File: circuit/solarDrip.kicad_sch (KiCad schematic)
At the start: 51 parts, among them J1 solar_charger, J10 Conn_01x08_Socket, J11 Logo_bot, J12 Logo_µc3, J13 solar_charger_smd, J2 batt, J3 solar, J4 pump, J5 soil, J6 water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

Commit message: resize R1-R4 to 0306
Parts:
- R1, R2, R3, R4: footprint Resistor_SMD:R_0402_1005Metric_Pad0.72x0.64mm_HandSolder -> Resistor_SMD:R_0603_1608Metric_Pad0.98x0.95mm_HandSolder
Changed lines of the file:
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@@
 			)
 		)
-		(property "Footprint" "Resistor_SMD:R_0402_1005Metric_Pad0.72x0.64mm_HandSolder"
+		(property "Footprint" "Resistor_SMD:R_0603_1608Metric_Pad0.98x0.95mm_HandSolder"
 			(at 66.802 123.19 90)
 			(effects
@@
 			)
 		)
-		(property "Footprint" "Resistor_SMD:R_0402_1005Metric_Pad0.72x0.64mm_HandSolder"
+		(property "Footprint" "Resistor_SMD:R_0603_1608Metric_Pad0.98x0.95mm_HandSolder"
 			(at 38.862 115.57 90)
 			(effects
@@
 			)
 		)
-		(property "Footprint" "Resistor_SMD:R_0402_1005Metric_Pad0.72x0.64mm_HandSolder"
+		(property "Footprint" "Resistor_SMD:R_0603_1608Metric_Pad0.98x0.95mm_HandSolder"
 			(at 38.862 123.19 90)
 			(effects
@@
 			)
 		)
-		(property "Footprint" "Resistor_SMD:R_0402_1005Metric_Pad0.72x0.64mm_HandSolder"
+		(property "Footprint" "Resistor_SMD:R_0603_1608Metric_Pad0.98x0.95mm_HandSolder"
 			(at 66.802 115.57 90)
 			(effects

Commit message: resize R5-R9 to 0306
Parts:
- R5, R6, R7, R8, R9: footprint Resistor_SMD:R_0402_1005Metric_Pad0.72x0.64mm_HandSolder -> Resistor_SMD:R_0603_1608Metric_Pad0.98x0.95mm_HandSolder
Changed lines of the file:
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@@
 			)
 		)
-		(property "Footprint" "Resistor_SMD:R_0402_1005Metric_Pad0.72x0.64mm_HandSolder"
+		(property "Footprint" "Resistor_SMD:R_0603_1608Metric_Pad0.98x0.95mm_HandSolder"
 			(at 154.178 96.52 90)
 			(effects
@@
 			)
 		)
-		(property "Footprint" "Resistor_SMD:R_0402_1005Metric_Pad0.72x0.64mm_HandSolder"
+		(property "Footprint" "Resistor_SMD:R_0603_1608Metric_Pad0.98x0.95mm_HandSolder"
 			(at 256.032 114.3 90)
 			(effects
@@
 			)
 		)
-		(property "Footprint" "Resistor_SMD:R_0402_1005Metric_Pad0.72x0.64mm_HandSolder"
+		(property "Footprint" "Resistor_SMD:R_0603_1608Metric_Pad0.98x0.95mm_HandSolder"
 			(at 211.582 115.57 90)
 			(effects
@@
 			)
 		)
-		(property "Footprint" "Resistor_SMD:R_0402_1005Metric_Pad0.72x0.64mm_HandSolder"
+		(property "Footprint" "Resistor_SMD:R_0603_1608Metric_Pad0.98x0.95mm_HandSolder"
 			(at 147.32 93.218 90)
 			(effects
@@
 			)
 		)
-		(property "Footprint" "Resistor_SMD:R_0402_1005Metric_Pad0.72x0.64mm_HandSolder"
+		(property "Footprint" "Resistor_SMD:R_0603_1608Metric_Pad0.98x0.95mm_HandSolder"
 			(at 220.472 115.57 90)
 			(effects

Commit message: add logo symbols
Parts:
- J11, J12: symbol Connector:Conn_01x01_Pin -> logos:logo
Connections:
- net GND: no longer J11.1 (Pin_1), J12.1 (Pin_1)
- no-connect marks 4 -> 5
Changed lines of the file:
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@@
 		(at 209.55 114.3)
 	)
+	(no_connect
+		(at 269.24 151.13)
+	)
 	(wire
 		(pts
@@
 	)
 	(symbol
-		(lib_id "Connector:Conn_01x01_Pin")
-		(at 247.65 151.13 0)
+		(lib_id "logos:logo")
+		(at 238.76 149.86 0)
 		(unit 1)
 		(exclude_from_sim no)
@@
 		(on_board yes)
 		(dnp no)
-		(fields_autoplaced yes)
 		(property "Reference" "J11"
-			(at 248.285 146.05 0)
+			(at 242.57 148.5899 0)
 			(effects
 				(font
 					(size 1.27 1.27)
 				)
+				(justify left)
 			)
 		)
 		(property "Value" "Logo_bot"
-			(at 248.285 148.59 0)
+			(at 234.442 146.05 0)
 			(effects
 				(font
 					(size 1.27 1.27)
 				)
+				(justify left)
 			)
 		)
 		(property "Footprint" "my_footprints:logo_solardrip"
-			(at 247.65 151.13 0)
+			(at 238.76 149.86 0)
 			(effects
 				(font
@@
 		)
 		(property "Datasheet" "~"
-			(at 247.65 151.13 0)
+			(at 238.76 149.86 0)
 			(effects
 				(font
@@
 		)
 		(property "Description" "Generic connector, single row, 01x01, script generated"
-			(at 247.65 151.13 0)
+			(at 238.76 149.86 0)
 			(effects
 				(font
@@
 			)
 		)
-		(pin "1"
-		)
 		(instances
 			(project "solarDrip"
@@
 	)
 	(symbol
-		(lib_id "Connector:Conn_01x01_Pin")
-		(at 264.16 151.13 0)
+		(lib_id "logos:logo")
+		(at 251.46 149.86 0)
 		(unit 1)
 		(exclude_from_sim no)
@@
 		(on_board yes)
 		(dnp no)
-		(fields_autoplaced yes)
 		(property "Reference" "J12"
-			(at 264.795 146.05 0)
+			(at 255.27 148.5899 0)
 			(effects
 				(font
 					(size 1.27 1.27)
 				)
+				(justify left)
 			)
 		)
 		(property "Value" "Logo_µc3"
-			(at 264.795 148.59 0)
+			(at 247.65 146.05 0)
 			(effects
 				(font
 					(size 1.27 1.27)
 				)
+				(justify left)
 			)
 		)
 		(property "Footprint" "my_footprints:muccc_logo"
-			(at 264.16 151.13 0)
+			(at 251.46 149.86 0)
 			(effects
 				(font
@@
 		)
 		(property "Datasheet" "~"
-			(at 264.16 151.13 0)
+			(at 251.46 149.86 0)
 			(effects
 				(font
@@
 		)
 		(property "Description" "Generic connector, single row, 01x01, script generated"
-			(at 264.16 151.13 0)
+			(at 251.46 149.86 0)
 			(effects
 				(font
@@
 			)
 		)
-		(pin "1"
-		)
 		(instances
 			(project "solarDrip"
@@
 	)
 	(symbol
-		(lib_id "power:GND")
-		(at 269.24 151.13 0)
-		(unit 1)
-		(exclude_from_sim no)
-		(in_bom yes)
-		(on_board yes)
-		(dnp no)
-		(property "Reference" "#PWR023"
-			(at 269.24 157.48 0)
-			(effects
-				(font
-					(size 1.27 1.27)
-				)
-				(hide yes)
-			)
-		)
-		(property "Value" "GND"
-			(at 269.24 156.21 0)
-			(effects
-				(font
-					(size 1.27 1.27)
-				)
-			)
-		)
-		(property "Footprint" ""
-			(at 269.24 151.13 0)
-			(effects
-				(font
-					(size 1.27 1.27)
-				)
-				(hide yes)
-			)
-		)
-		(property "Datasheet" ""
-			(at 269.24 151.13 0)
-			(effects
-				(font
-					(size 1.27 1.27)
-				)
-				(hide yes)
-			)
-		)
-		(property "Description" "Power symbol creates a global label with name \"GND\" , ground"
-			(at 269.24 151.13 0)
-			(effects
-				(font
-					(size 1.27 1.27)
-				)
-				(hide yes)
-			)
-		)
-		(pin "1"
-		)
-		(instances
-			(project "solarDrip"
-				(path "/6377a484-fa16-4056-97a2-452f2b7af807"
-					(reference "#PWR023")
-					(unit 1)
-				)
-			)
-		)
-	)
-	(symbol
 		(lib_id "Device:R")
 		(at 40.64 123.19 0)
@@
 					(unit 1)
 				)
-			)
-		)
-	)
-	(symbol
-		(lib_id "power:GND")
-		(at 252.73 151.13 0)
-		(unit 1)
-		(exclude_from_sim no)
-		(in_bom yes)
-		(on_board yes)
-		(dnp no)
-		(property "Reference" "#PWR022"
-			(at 252.73 157.48 0)
-			(effects
-				(font
-					(size 1.27 1.27)
-				)
-				(hide yes)
-			)
-		)
-		(property "Value" "GND"
-			(at 252.73 156.21 0)
-			(effects
-				(font
-					(size 1.27 1.27)
-				)
-			)
-		)
-		(property "Footprint" ""
-			(at 252.73 151.13 0)
-			(effects
-				(font
-					(size 1.27 1.27)
-				)
-				(hide yes)
-			)
-		)
-		(property "Datasheet" ""
-			(at 252.73 151.13 0)
-			(effects
-				(font
-					(size 1.27 1.27)
-				)
-				(hide yes)
-			)
-		)
-		(property "Description" "Power symbol creates a global label with name \"GND\" , ground"
-			(at 252.73 151.13 0)
-			(effects
-				(font
-					(size 1.27 1.27)
-				)
-				(hide yes)
-			)
-		)
-		(pin "1"
-		)
-		(instances
-			(project "solarDrip"
-				(path "/6377a484-fa16-4056-97a2-452f2b7af807"
-					(reference "#PWR022")
-					(unit 1)
-				)

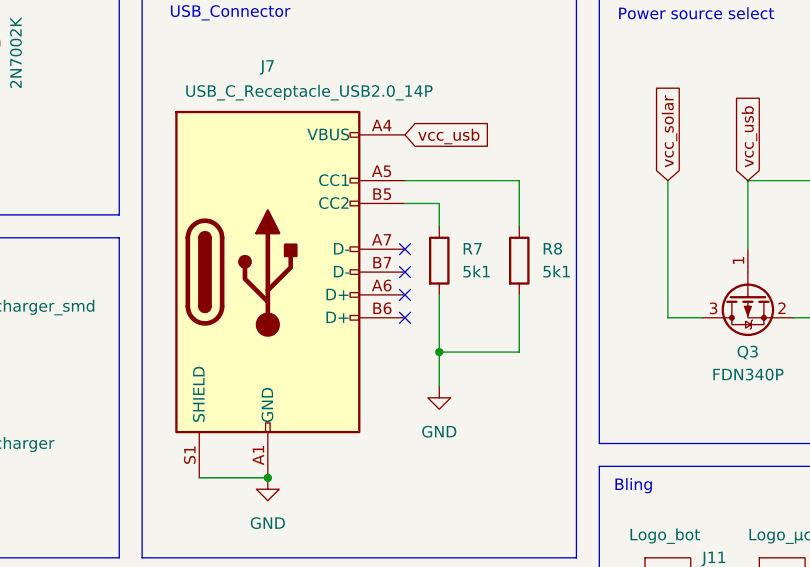
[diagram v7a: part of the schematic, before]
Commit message: fix usb net
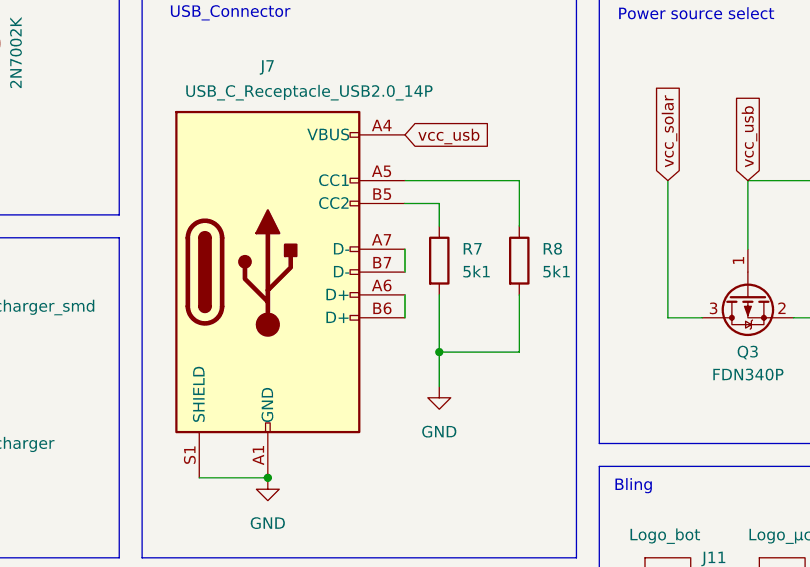
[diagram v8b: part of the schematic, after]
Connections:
- net at J7.A6 (D+): now also J7.B6 (D+)
- net at J7.A7 (D-): now also J7.B7 (D-)
- no-connect marks 5 -> 1
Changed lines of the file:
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@@
-	)
-	(no_connect
-		(at 209.55 121.92)
-	)
-	(no_connect
-		(at 209.55 119.38)
-	)
-	(no_connect
-		(at 209.55 116.84)
-	)
-	(no_connect
-		(at 209.55 114.3)
 	)
 	(no_connect
@@
 	(wire
 		(pts
+			(xy 209.55 119.38) (xy 209.55 121.92)
+		)
+		(stroke
+			(width 0)
+			(type default)
+		)
+	)
+	(wire
+		(pts
 			(xy 209.55 106.68) (xy 222.25 106.68)
 		)
@@
 		)
 		(stroke
+			(width 0)
+			(type default)
+		)
+	)
+	(wire
+		(pts
+			(xy 209.55 114.3) (xy 209.55 116.84)
+		)
+		(stroke
